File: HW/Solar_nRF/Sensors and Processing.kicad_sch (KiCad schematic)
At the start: 10 parts, among them J13 Conn_02x03_Odd_Even, U3 MDBT42TV, U4 TMP112xxDRL, Y1 ABS07-32.768KHZ-T

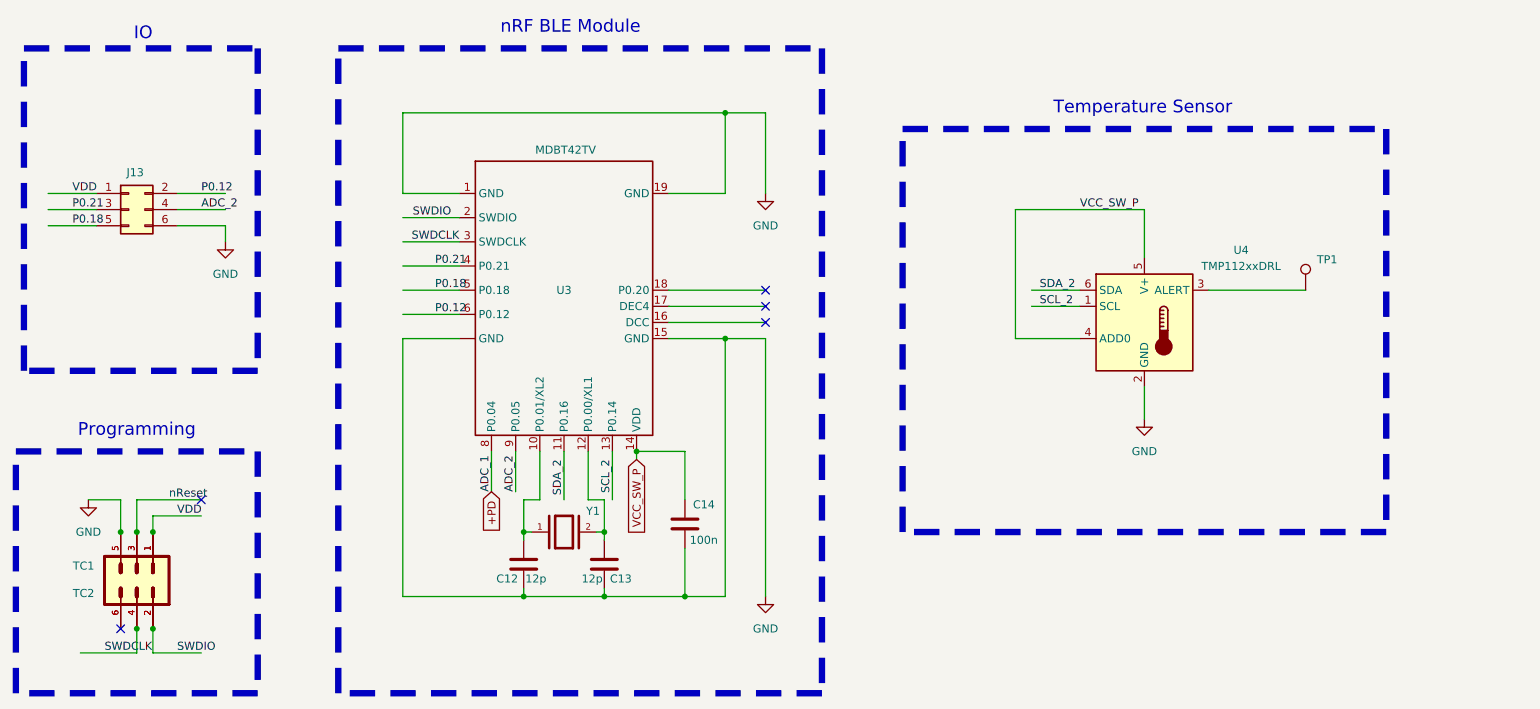
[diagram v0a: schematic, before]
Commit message: Updated SCH & PCB based with fixes found during development
Inverted bat_ok signal
Cleaned up layout, removing solar array and replacing with a single photodiode
Connected nRF to +V programming pad
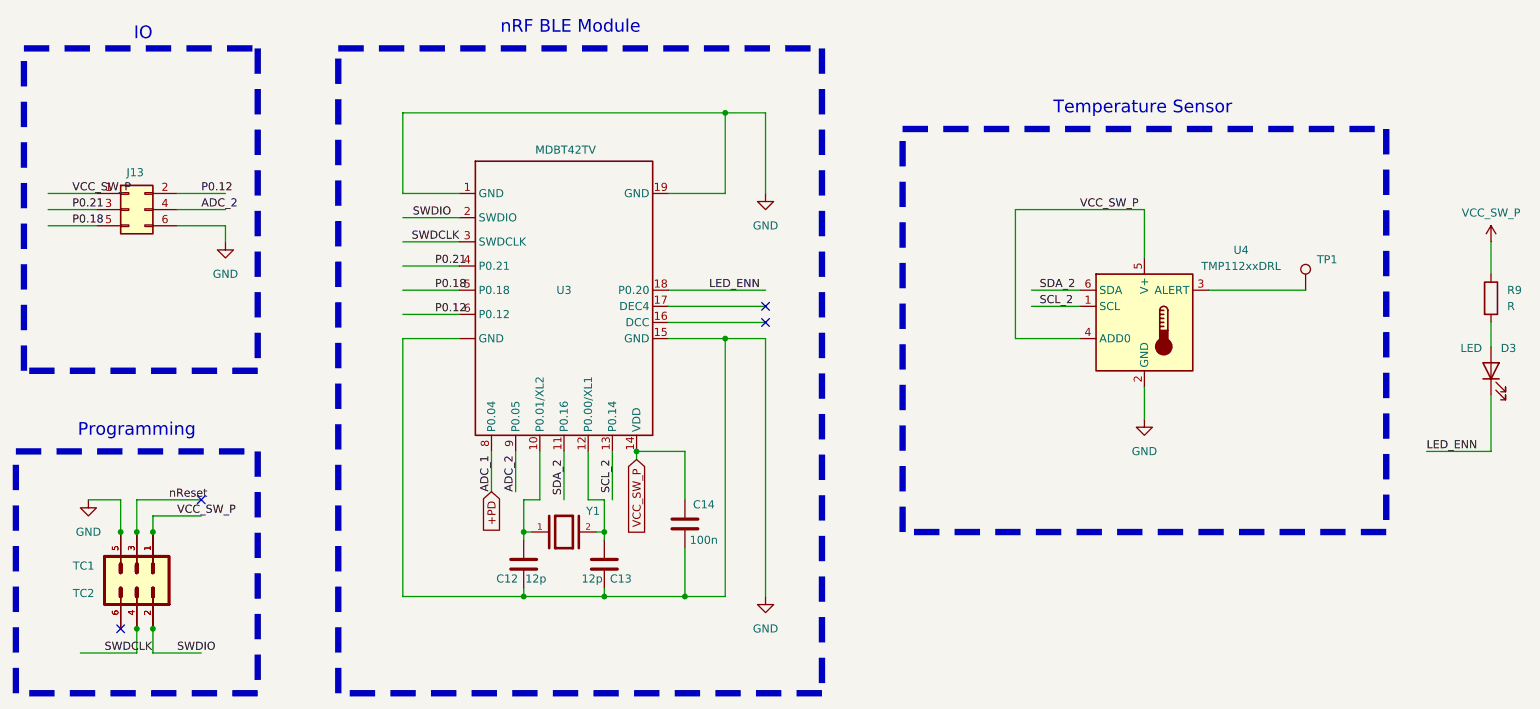
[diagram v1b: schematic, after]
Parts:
- added D3: LED, LED_SMD:LED_0805_2012Metric_Pad1.15x1.40mm_HandSolder, symbol Device:LED
- added R9: R, Resistor_SMD:R_0805_2012Metric_Pad1.20x1.40mm_HandSolder, symbol Device:R
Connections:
- net VDD is gone; now on net VCC_SW_P: J13.1 (Pin_1), TC1.1, TC2.1
- net VCC_SW_P: now also R9.1
- net LED_ENN: now reaches U3.18 (P0.20)
- net LED_ENN: now also D3.1 (K)
- new net: D3.2 (A), R9.2
- no-connect marks 5 -> 4
